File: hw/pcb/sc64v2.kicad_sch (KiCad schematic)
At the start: 94 parts, among them J1 DX07S016JA3R1500, J2 Conn_01x03_Male, J3 TC2050-FP, J4 104031-0811, SW1 TS07-667-37-BK-160-SMT, U1 TC1264-3.3VDB, U2 TPS2111A, U3 FT232HL, U4 93AA56Bx-x/OT, U5 W25Q128JVSIQ, U6 STM32G030F6P6, U7 MCP7940N-x/ST, U8 LCMXO2-7000Hx-xTG144x, U9 IS42S16320F-7TL, X1 ECS-3225MV-120-CN, X2 ECS-3225MV-500-BN, Y1 FC-135

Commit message: updated component values
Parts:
- C21, C22: value 12pF -> 7pF
- R1: value 10k -> 1k
- R12: value 3.3k -> 10k
- R18: value 470R -> 1k
- R2: value 3.3k -> 330R
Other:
- moved on the sheet: C4, C5, C6, R1, R19, R2, R3, U2

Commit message: button and naming
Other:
- title: SummerCart64 -> SC64
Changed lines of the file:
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@@
   (paper "A2")
   (title_block
-    (title "SummerCart64")
+    (title "SC64")
     (date "2022-05-15")
     (rev "2.0")

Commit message: pc software done
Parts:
- R8: value 12k -> 10k
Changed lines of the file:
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@@
       (effects (font (size 1.27 1.27)) (justify right))
     )
-    (property "Value" "12k" (id 1) (at 196.85 386.0799 0)
+    (property "Value" "10k" (id 1) (at 196.85 386.0799 0)
       (effects (font (size 1.27 1.27)) (justify right))
     )
@@
     )
     (path "/d1984805-4314-4f1c-9ab1-479802945b94"
-      (reference "R8") (unit 1) (value "12k") (footprint "Resistor_SMD:R_0603_1608Metric")
+      (reference "R8") (unit 1) (value "10k") (footprint "Resistor_SMD:R_0603_1608Metric")
     )
     (path "/38f041d3-336d-4c45-9e25-efeece1e2340"

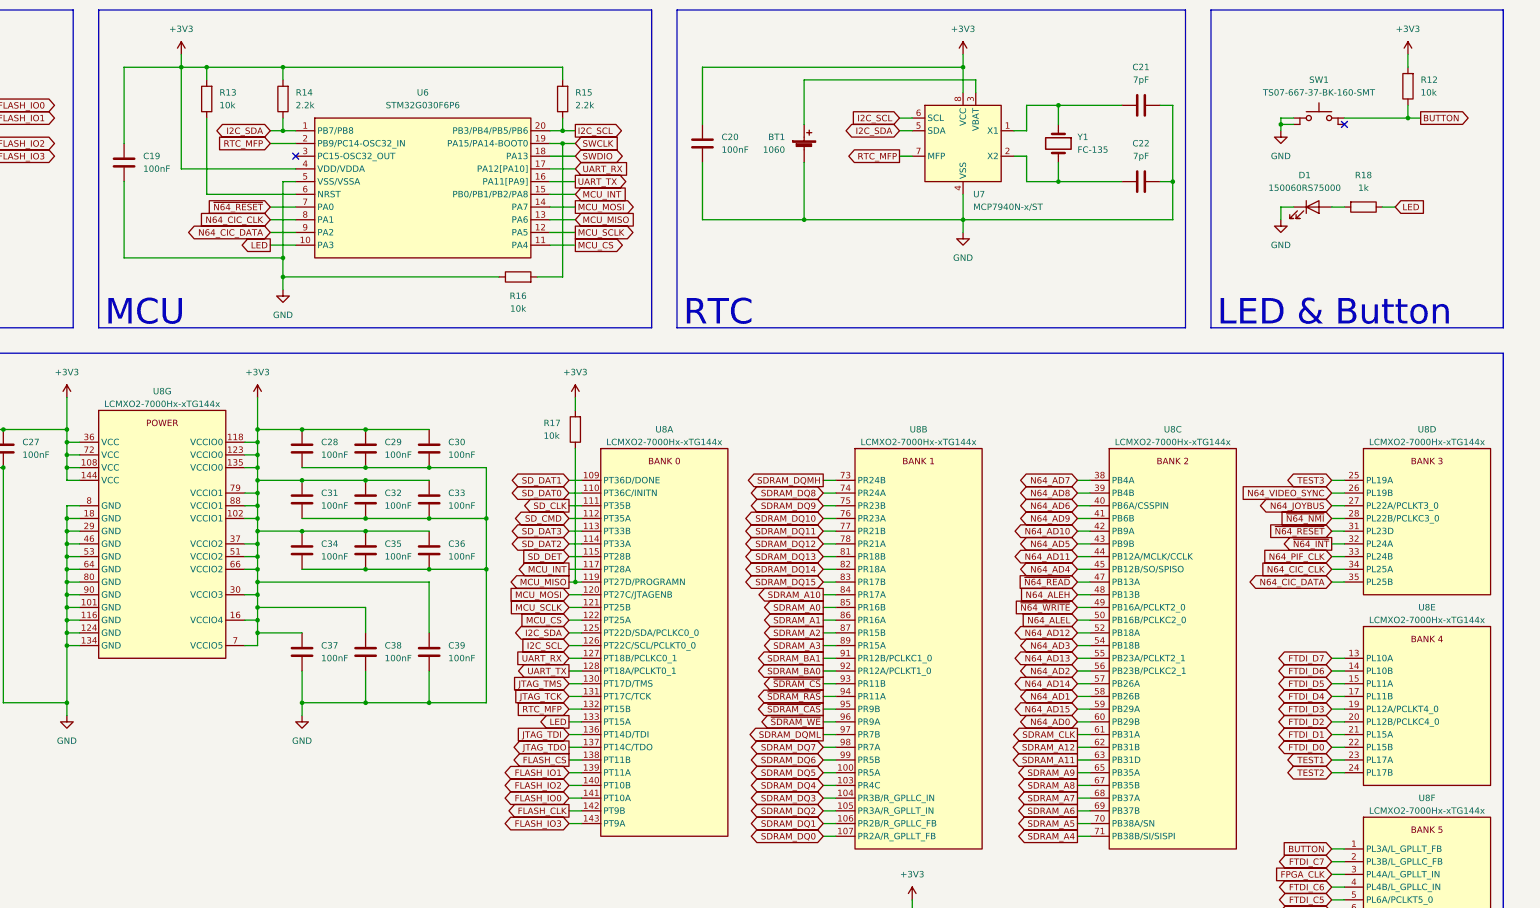
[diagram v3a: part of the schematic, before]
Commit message: [SC64][HW] Updated PCB BOM and GitHub address
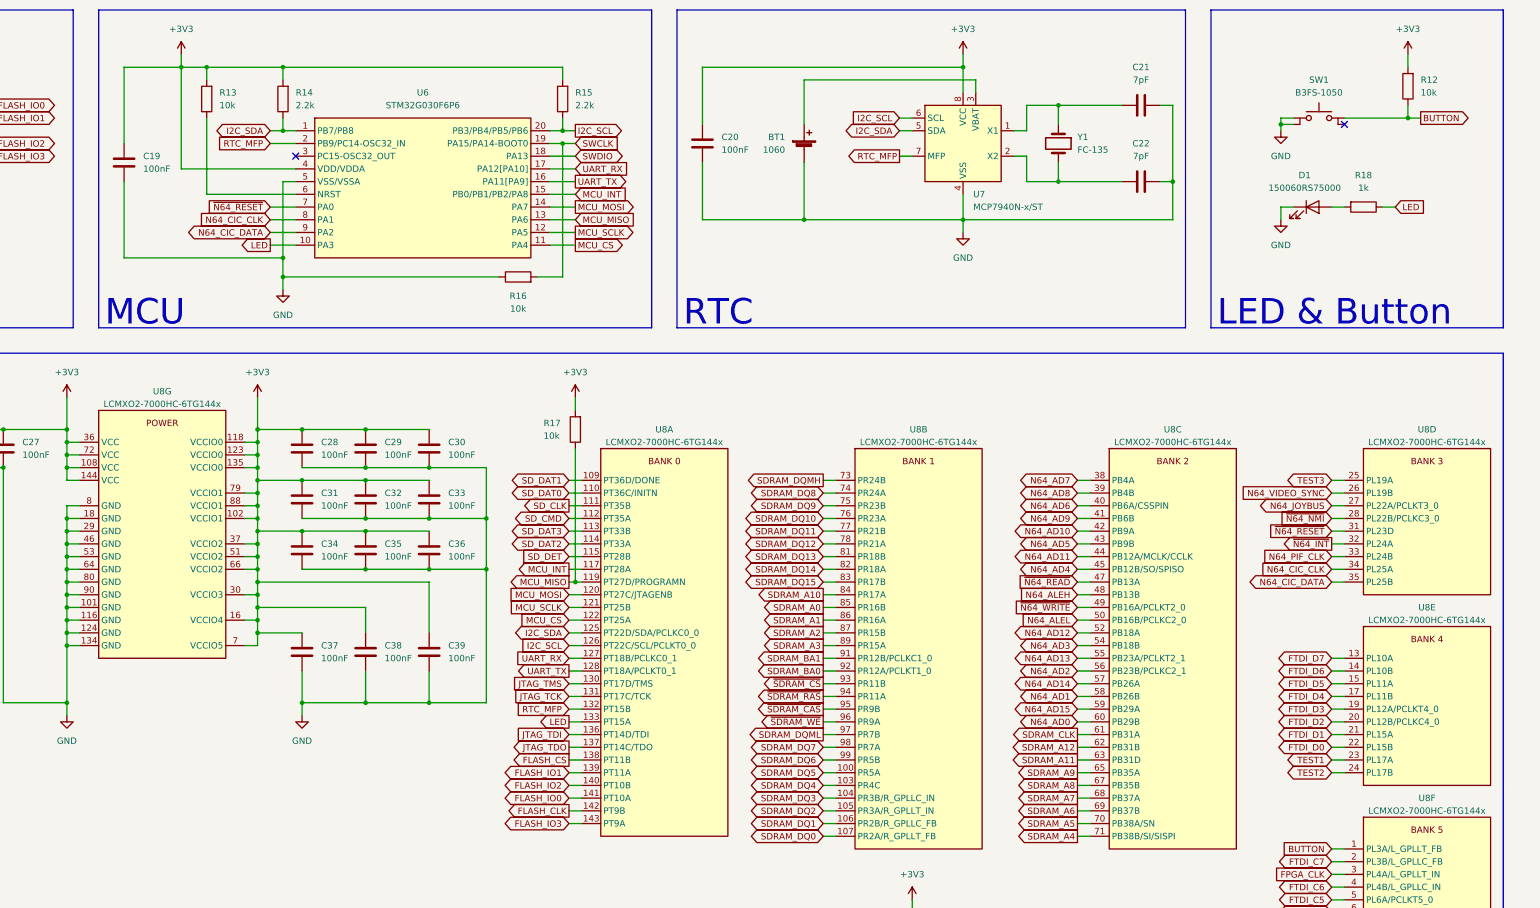
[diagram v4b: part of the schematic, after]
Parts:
- 3V1, GND1, J3, J_N1, TP1, TP2, TP3: Notes (none) -> Not in BOM
- J2: Notes (none) -> Not in BOM; now left out of the parts list
- L1, L2: Notes (none) -> Use ferrite bead
- SW1: value TS07-667-37-BK-160-SMT -> B3FS-1050; footprint Button_Switch_SMD:SW_SPST_Omron_B3FS-101xP -> custom:SW_SPST_Omron_B3FS-105xP_custom; Notes (none) -> Recommended button cap: B32-2010
- U1: Notes (none) -> Can be replaced by: AZ1117CH2-3.3
- U4: Notes (none) -> Can be replaced by: 93LC56Bx-x/OT or similar
- U7: Notes (none) -> Can be replaced by: MCP79410/MCP79411/MCP79412
- U8: value LCMXO2-7000Hx-xTG144x -> LCMXO2-7000HC-6TG144x; Notes (none) -> Speed grade 6 is required. Last letter (C/I) is not importa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

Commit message: [SC64][HW] Added PCB BOM
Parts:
- D1: Notes (none) -> Can be replaced by: any 0603 LED
- SW1: footprint custom:SW_SPST_Omron_B3FS-105xP_custom -> Button_Switch_SMD:SW_SPST_Omron_B3FS-105xP; symbol sc64v2:Tactile_Switch -> Switch:SW_Push
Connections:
- net BUTTON: now also SW1.2; no longer SW1.3
- net GND: no longer SW1.2
- no-connect marks 14 -> 13

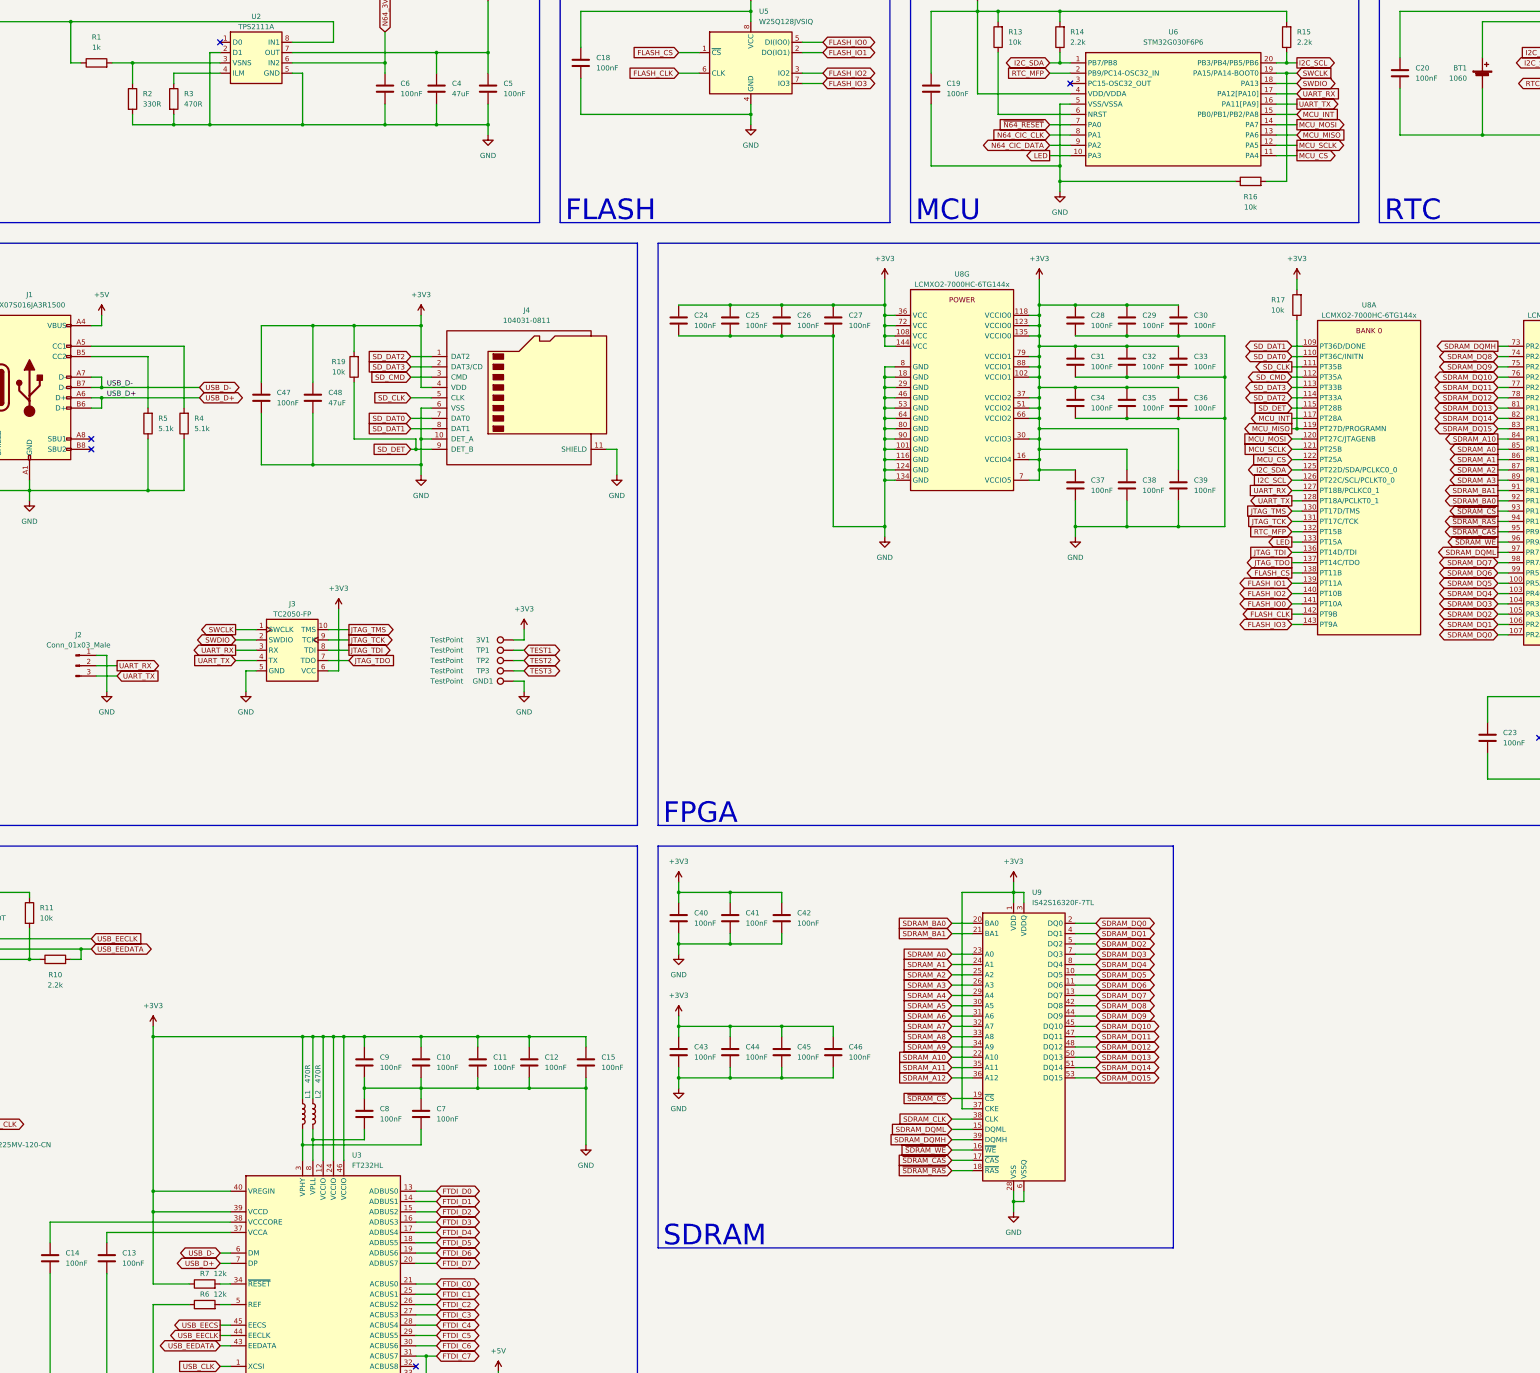
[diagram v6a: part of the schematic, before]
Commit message: [SC64][HW] Changed battery holder from 1060 to 1058 + minor PCB improvements
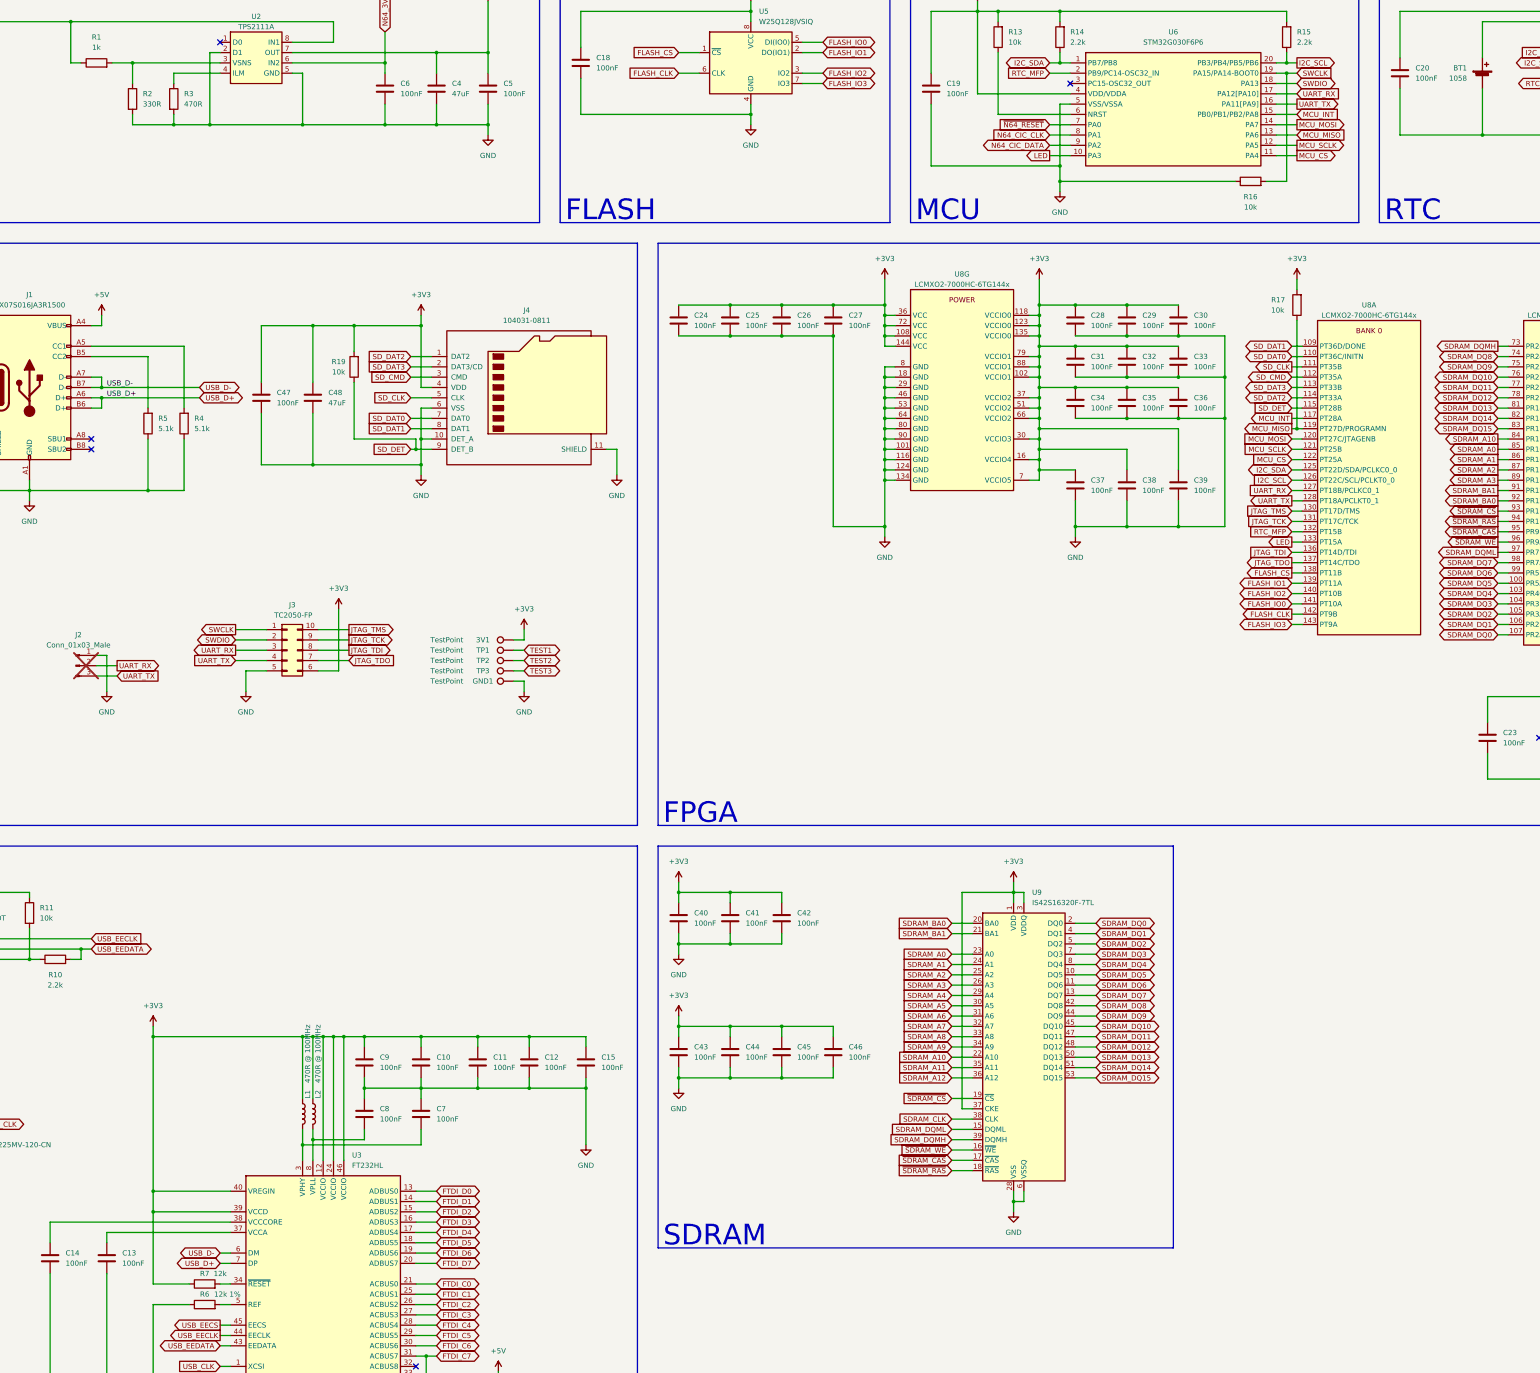
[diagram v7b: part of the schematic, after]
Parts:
- BT1: value 1060 -> 1058; footprint Battery:BatteryHolder_Keystone_1060_1x2032 -> Battery:BatteryHolder_Keystone_1058_1x2032
- J2: now not fitted
- J3: footprint sc64v2:TC2050-FP -> Connector:Tag-Connect_TC2050-IDC-FP_2x05_P1.27mm_Vertical; symbol sc64v2:TC2050-FP -> Connector_Generic:Conn_02x05_Counter_Clockwise
- L1, L2: value 470R -> 470R @ 100MHz
- R6: value 12k -> 12k 1%
- Y1: Notes (none) -> Use standard 32.768kHz crystal
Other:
- company: Polprzewodnikowy -> Mateusz Faderewski
- title: SC64 -> SummerCart64
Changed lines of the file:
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@@
 	(paper "A2")
 	(title_block
-		(title "SC64")
-		(date "2023-02-12")
-		(rev "2.0a")
-		(company "Polprzewodnikowy")
+		(title "SummerCart64")
+		(date "2024-08-11")
+		(rev "2.1")
+		(company "Mateusz Faderewski")
 	)
 	(junction
@@
 	(wire
 		(pts
-			(xy 129.54 184.15) (xy 134.62 184.15)
+			(xy 129.54 184.15) (xy 137.16 184.15)
 		)
 		(stroke
@@
 	(wire
 		(pts
-			(xy 152.4 181.61) (xy 157.48 181.61)
-		)
-		(stroke
-			(width 0)
-			(type default)
-		)
-	)
-	(wire
-		(pts
 			(xy 48.26 39.37) (xy 48.26 57.15)
 		)
@@
 	(wire
 		(pts
-			(xy 152.4 184.15) (xy 157.48 184.15)
-		)
-		(stroke
-			(width 0)
-			(type default)
-		)
-	)
-	(wire
-		(pts
 			(xy 327.66 127) (xy 327.66 124.46)
 		)
@@
 	(wire
 		(pts
+			(xy 149.86 181.61) (xy 157.48 181.61)
+		)
+		(stroke
+			(width 0)
+			(type default)
+		)
+	)
+	(wire
+		(pts
 			(xy 21.59 143.51) (xy 21.59 146.05)
 		)
@@
 	(wire
 		(pts
+			(xy 149.86 186.69) (xy 157.48 186.69)
+		)
+		(stroke
+			(width 0)
+			(type default)
+		)
+	)
+	(wire
+		(pts
 			(xy 542.29 203.2) (xy 544.83 203.2)
 		)
@@
 	(wire
 		(pts
-			(xy 129.54 186.69) (xy 134.62 186.69)
+			(xy 129.54 186.69) (xy 137.16 186.69)
 		)
 		(stroke
@@
 	(wire
 		(pts
-			(xy 129.54 181.61) (xy 134.62 181.61)
+			(xy 129.54 181.61) (xy 137.16 181.61)
 		)
 		(stroke
@@
 	(wire
 		(pts
-			(xy 152.4 186.69) (xy 157.48 186.69)
-		)
-		(stroke
-			(width 0)
-			(type default)
-		)
-	)
-	(wire
-		(pts
 			(xy 468.63 59.69) (xy 510.54 59.69)
 		)
@@
 	(wire
 		(pts
-			(xy 152.4 189.23) (xy 157.48 189.23)
-		)
-		(stroke
-			(width 0)
-			(type default)
-		)
-	)
-	(wire
-		(pts
 			(xy 491.49 127) (xy 494.03 127)
 		)
@@
 	(wire
 		(pts
-			(xy 129.54 189.23) (xy 134.62 189.23)
+			(xy 129.54 189.23) (xy 137.16 189.23)
 		)
 		(stroke
@@
 	(wire
 		(pts
-			(xy 134.62 191.77) (xy 132.08 191.77)
+			(xy 132.08 191.77) (xy 137.16 191.77)
 		)
 		(stroke
@@
 	(wire
 		(pts
+			(xy 149.86 189.23) (xy 157.48 189.23)
+		)
+		(stroke
+			(width 0)
+			(type default)
+		)
+	)
+	(wire
+		(pts
 			(xy 336.55 119.38) (xy 349.25 119.38)
 		)
@@
 	(wire
 		(pts
+			(xy 149.86 184.15) (xy 157.48 184.15)
+		)
+		(stroke
+			(width 0)
+			(type default)
+		)
+	)
+	(wire
+		(pts
 			(xy 44.45 113.03) (xy 46.99 113.03)
 		)
@@
 	(wire
 		(pts
-			(xy 194.31 391.16) (xy 166.37 391.16)
+			(xy 149.86 191.77) (xy 154.94 191.77)
 		)
 		(stroke
@@
 	(wire
 		(pts
-			(xy 325.12 144.78) (xy 327.66 144.78)
+			(xy 194.31 391.16) (xy 166.37 391.16)
 		)
 		(stroke
@@
 	(wire
 		(pts
-			(xy 146.05 388.62) (xy 146.05 391.16)
+			(xy 325.12 144.78) (xy 327.66 144.78)
 		)
 		(stroke
@@
 	(wire
 		(pts
-			(xy 152.4 191.77) (xy 154.94 191.77)
+			(xy 146.05 388.62) (xy 146.05 391.16)
 		)
 		(stroke
@@
 			)
 		)
-		(property "Value" "12k"
-			(at 125.73 345.44 90)
+		(property "Value" "12k 1%"
+			(at 127.508 345.44 90)
 			(effects
 				(font
@@
 			)
 		)
+		(property "exclude_from_bom" ""
+			(at 0 205.74 0)
+			(effects
+				(font
+					(size 1.27 1.27)
+				)
+				(hide yes)
+			)
+		)
 		(pin "1"
 		)
@@
 		(in_bom no)
 		(on_board yes)
-		(dnp no)
+		(dnp yes)
 		(fields_autoplaced yes)
 		(property "Reference" "J2"
@@
 			)
 		)
-		(property "Value" "1060"
+		(property "Value" "1058"
 			(at 433.07 45.72 0)
 			(effects
@@
 			)
 		)
-		(property "Footprint" "Battery:BatteryHolder_Keystone_1060_1x2032"
+		(property "Footprint" "Battery:BatteryHolder_Keystone_1058_1x2032"
 			(at 436.88 44.196 90)
 			(effects
@@
 			)
 		)
-		(property "Value" "470R"
+		(property "Value" "470R @ 100MHz"
 			(at 149.86 293.37 90)
 			(effects
@@
 	)
 	(symbol
-		(lib_id "sc64v2:TC2050-FP")
-		(at 143.51 179.07 0)
+		(lib_id "Connector_Generic:Conn_02x05_Counter_Clockwise")
+		(at 142.24 186.69 0)
 		(unit 1)
 		(exclude_from_sim no)
@@
 		(dnp no)
 		(property "Reference" "J3"
-			(at 143.51 175.26 0)
+			(at 143.51 175.514 0)
 			(effects
 				(font
@@
 		)
 		(property "Value" "TC2050-FP"
-			(at 143.51 177.8 0)
+			(at 143.764 178.054 0)
 			(effects
 				(font
@@
 			)
 		)
-		(property "Footprint" "sc64v2:TC2050-FP"
-			(at 143.51 184.15 0)
+		(property "Footprint" "Connector:Tag-Connect_TC2050-IDC-FP_2x05_P1.27mm_Vertical"
+			(at 142.24 191.77 0)
 			(effects
 				(font
@@
 		)
 		(property "Datasheet" ""
-			(at 143.51 184.15 0)
+			(at 142.24 191.77 0)
 			(effects
 				(font
@@
 		)
 		(property "Description" ""
-			(at 143.51 179.07 0)
+			(at 142.24 186.69 0)
 			(effects
 				(font
@@
 		)
 		(property "Notes" "Not in BOM"
-			(at 143.51 179.07 0)
+			(at 142.24 186.69 0)
+			(effects
+				(font
+					(size 1.27 1.27)
+				)
+				(hide yes)
+			)
+		)
+		(property "exclude_from_bom" ""
+			(at 0 373.38 0)
 			(effects
 				(font
@@
 			)
 		)
-		(property "Value" "470R"
+		(property "Value" "470R @ 100MHz"
 			(at 147.32 293.37 90)
 			(effects
@@
 			(effects
 				(font
+					(size 1.27 1.27)
+				)
+				(hide yes)
+			)
+		)
+		(property "Notes" "Use standard 32.768kHz crystal"
+			(at 487.68 44.45 90)
+			(effects
+				(font
